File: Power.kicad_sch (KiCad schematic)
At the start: 42 parts, among them J1 XT60_BAT, J102 E_STOP, Q1 SQJ459EP-T1_GE3, U1 LMR36520FADDA, U2 AP2112K-3.3

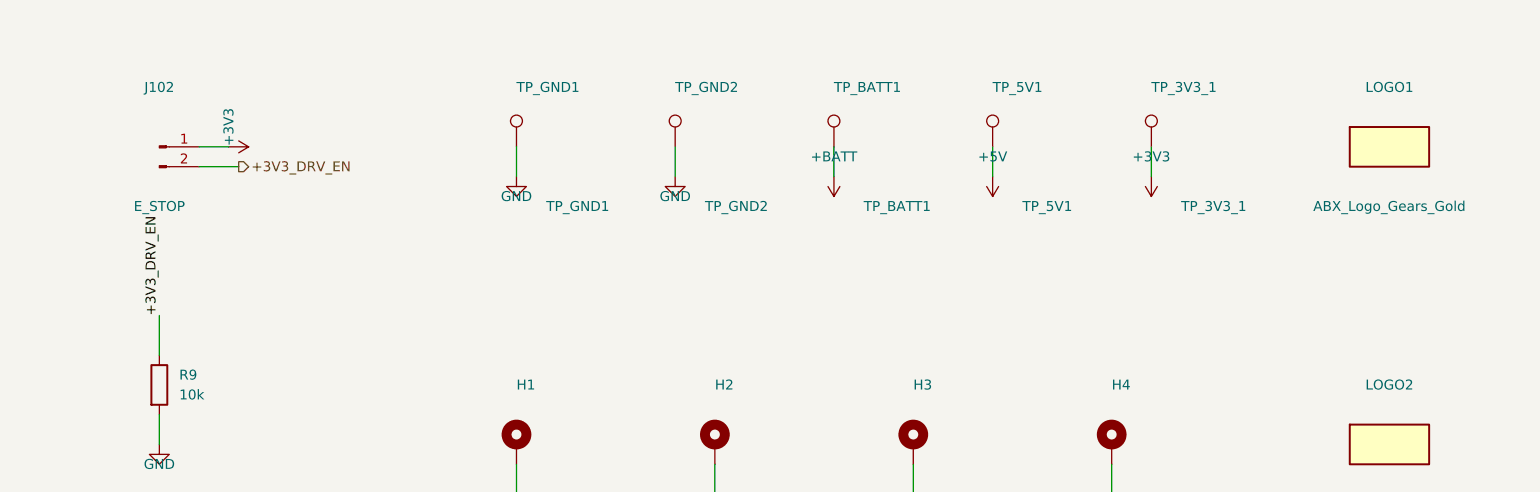
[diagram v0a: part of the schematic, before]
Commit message: Save Rev 1.2a three-axis checkpoint and audited JLCPCB exports
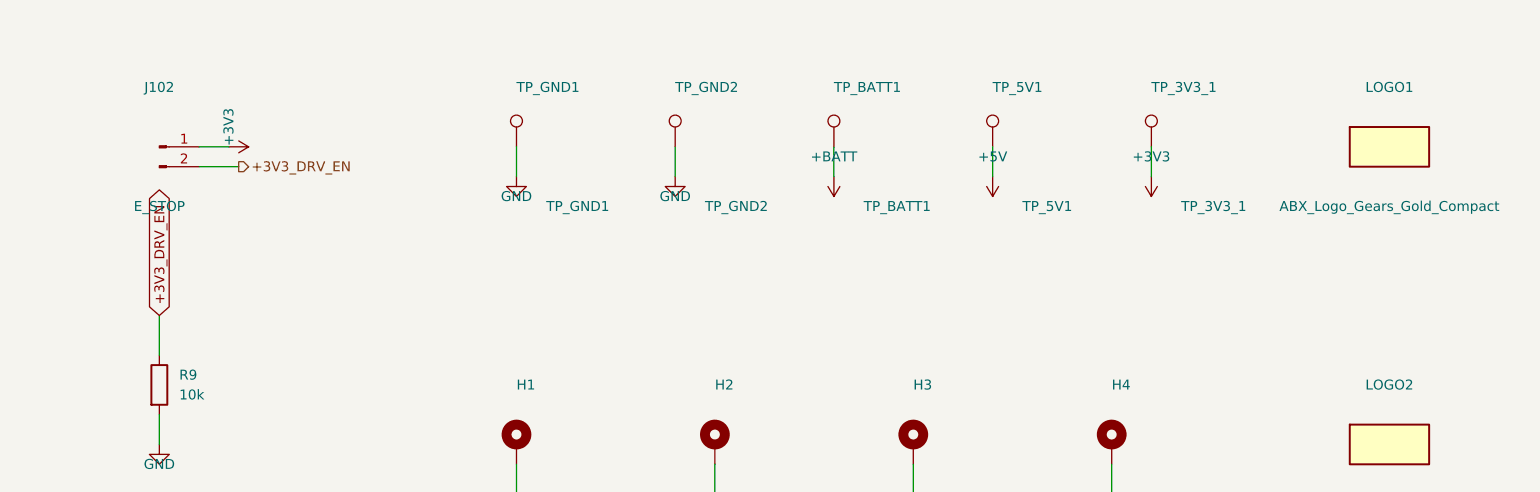
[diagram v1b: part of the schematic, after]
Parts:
- C1, C4, C6: LCSC (none) -> C14663
- C10: LCSC (none) -> C15850
- C2, C3: LCSC (none) -> C29823
- C5, C9: LCSC (none) -> C15849
- C7, C8: LCSC (none) -> C12891
- D1: LCSC (none) -> C14643
- D2: LCSC (none) -> C2863624
- F1: LCSC (none) -> C352820
- J1: LCSC (none) -> C98733
- J102: LCSC (none) -> C8465
- L1: LCSC (none) -> C177243
- LED_PWR_3V3_1, LED_PWR_5V1, LED_PWR_BATT1: LCSC (none) -> C12624
- LOGO1: value ABX_Logo_Gears_Gold -> ABX_Logo_Gears_Gold_Compact; footprint abx-footprints:ABX_Logo_Gears_Gold -> abx-footprints:ABX_Logo_Gears_Gold_Compact
- Q1: LCSC (none) -> C3289501
- R1: LCSC (none) -> C25819
- R2: LCSC (none) -> C22807
- R3, R9: LCSC (none) -> C25804
- R4: LCSC (none) -> C25803
- R5: LCSC (none) -> C25962
- R6: LCSC (none) -> C31850
- R7, R8: LCSC (none) -> C21190
- U1: LCSC (none) -> C1858395
- U2: LCSC (none) -> C51118

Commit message: Clear root project DRC findings and preserve explicit Ethernet draft status
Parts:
- J102: footprint TerminalBlock_Phoenix:TerminalBlock_Phoenix_MKDS-1,5-2-5.08_1x02_P5.08mm_Horizontal -> abx-footprints:ABX_J102_TerminalBlock_Phoenix_MKDS-1_5-2-5.08_1x02_P5.08mm_Horizontal
- TP_3V3_1: footprint TestPoint:TestPoint_Pad_D1.5mm -> abx-footprints:ABX_TP_3V3_1_TestPoint_Pad_D1.5mm
- TP_5V1: footprint TestPoint:TestPoint_Pad_D1.5mm -> abx-footprints:ABX_TP_5V1_TestPoint_Pad_D1.5mm
- TP_BATT1: footprint TestPoint:TestPoint_Pad_D1.5mm -> abx-footprints:ABX_TP_BATT1_TestPoint_Pad_D1.5mm
- TP_GND1: footprint TestPoint:TestPoint_Pad_D1.5mm -> abx-footprints:ABX_TP_GND1_TestPoint_Pad_D1.5mm
- TP_GND2: footprint TestPoint:TestPoint_Pad_D1.5mm -> abx-footprints:ABX_TP_GND2_TestPoint_Pad_D1.5mm
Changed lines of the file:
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@@
 			)
 		)
-		(property "Footprint" "TerminalBlock_Phoenix:TerminalBlock_Phoenix_MKDS-1,5-2-5.08_1x02_P5.08mm_Horizontal"
+		(property "Footprint" "abx-footprints:ABX_J102_TerminalBlock_Phoenix_MKDS-1_5-2-5.08_1x02_P5.08mm_Horizontal"
 			(at 198.12 215.9 0)
 			(effects
@@
 			)
 		)
-		(property "Footprint" "TestPoint:TestPoint_Pad_D1.5mm"
+		(property "Footprint" "abx-footprints:ABX_TP_GND1_TestPoint_Pad_D1.5mm"
 			(at 243.84 215.9 0)
 			(effects
@@
 			)
 		)
-		(property "Footprint" "TestPoint:TestPoint_Pad_D1.5mm"
+		(property "Footprint" "abx-footprints:ABX_TP_GND2_TestPoint_Pad_D1.5mm"
 			(at 264.16 215.9 0)
 			(effects
@@
 			)
 		)
-		(property "Footprint" "TestPoint:TestPoint_Pad_D1.5mm"
+		(property "Footprint" "abx-footprints:ABX_TP_BATT1_TestPoint_Pad_D1.5mm"
 			(at 284.48 215.9 0)
 			(effects
@@
 			)
 		)
-		(property "Footprint" "TestPoint:TestPoint_Pad_D1.5mm"
+		(property "Footprint" "abx-footprints:ABX_TP_5V1_TestPoint_Pad_D1.5mm"
 			(at 304.8 215.9 0)
 			(effects
@@
 			)
 		)
-		(property "Footprint" "TestPoint:TestPoint_Pad_D1.5mm"
+		(property "Footprint" "abx-footprints:ABX_TP_3V3_1_TestPoint_Pad_D1.5mm"
 			(at 325.12 215.9 0)
 			(effects
